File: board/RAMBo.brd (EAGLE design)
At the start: 104.1 x 102.9 mm, 262 parts, among them Q1 PSMN7R0-60YS, Q2 PSMN7R0-60YS, Q3 PSMN7R0-60YS, Q4 IRLML6346TRPBF, Q5 PSMN7R0-60YS, Q8 IRLML6346TRPBF, U1 ATMEGA32U2-MUR, U10 ADUM7441, U2 ATMEGA2560-16AU, U3 TPS54332DDA, U4 AD5206, U5 A4982, U6 A4982, U7 A4982, U8 A4982, U9 A4982, X1 C-GRID-02-70543, X10 C-GRID-04-70543, X11 MSTBV10, X12 SPI, X13 EXT-2, X14 C-GRID-04-70543, X15 C-GRID-04-70543, X16 32u2 EXT, X17 3x2M, X18 3x2M, X19 Analog-Ext, X2 USB B-TH, X20 M05PTH, X21 C-GRID-03-70543, X22 C-GRID-03-70543, X23 C-GRID-03-70543, X24 C-GRID-03-70543, X25 C-GRID-03-70543, X26 C-GRID-03-70543, X27 C-GRID-02-70543, X28 C-GRID-02-70543, X29 C-GRID-02-70543, X3 C-GRID-02-70543, X30 C-GRID-02-70543, X31 M05PTH, X32 M05PTH, X33 MSTBA6, X34 PWM_EXT, X39 M05X2PTH, X4 C-GRID-04-70543, X5 C-GRID-02-70543, X6 C-GRID-04-70543, X7 C-GRID-04-70543, X8 C-GRID-04-70543, X9 C-GRID-02-70543, Y1 16MHz KX-7, Y2 16MHz KX-7

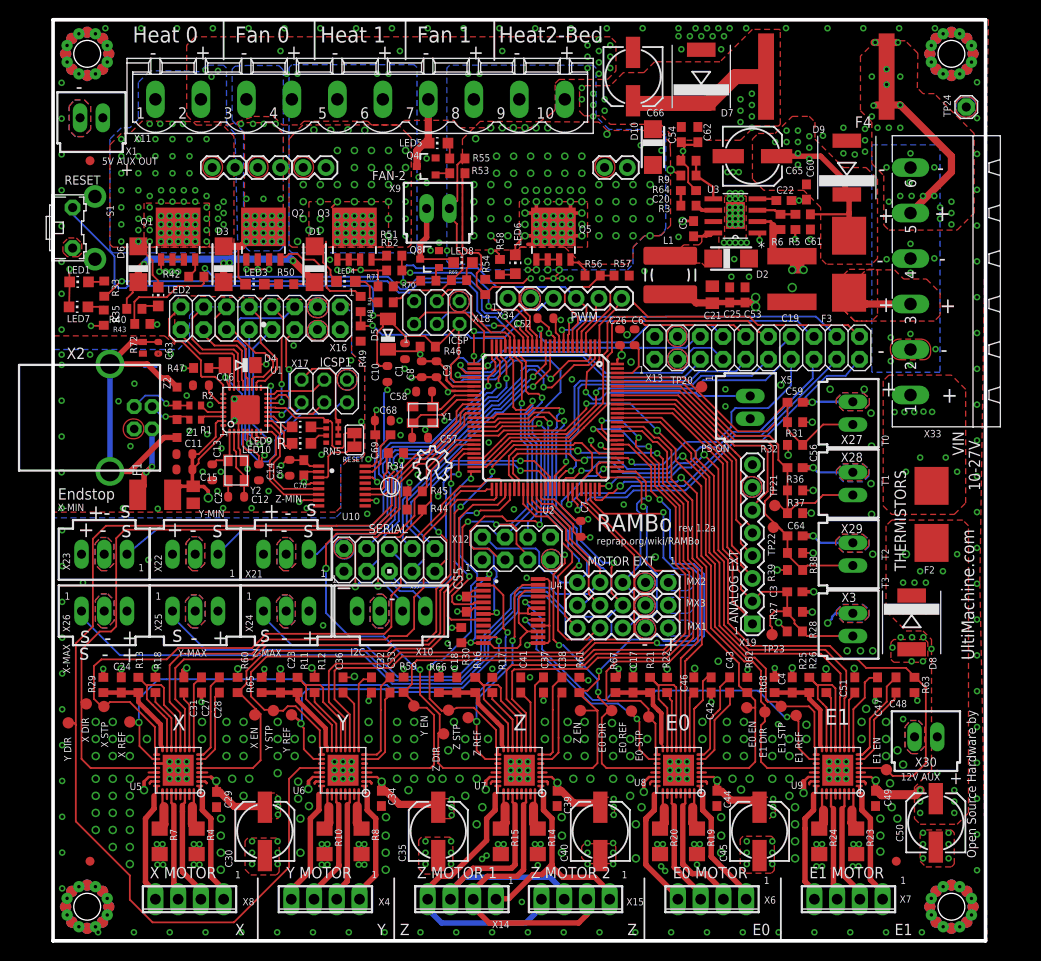
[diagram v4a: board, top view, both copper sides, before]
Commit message: remove solder pads under mount holes
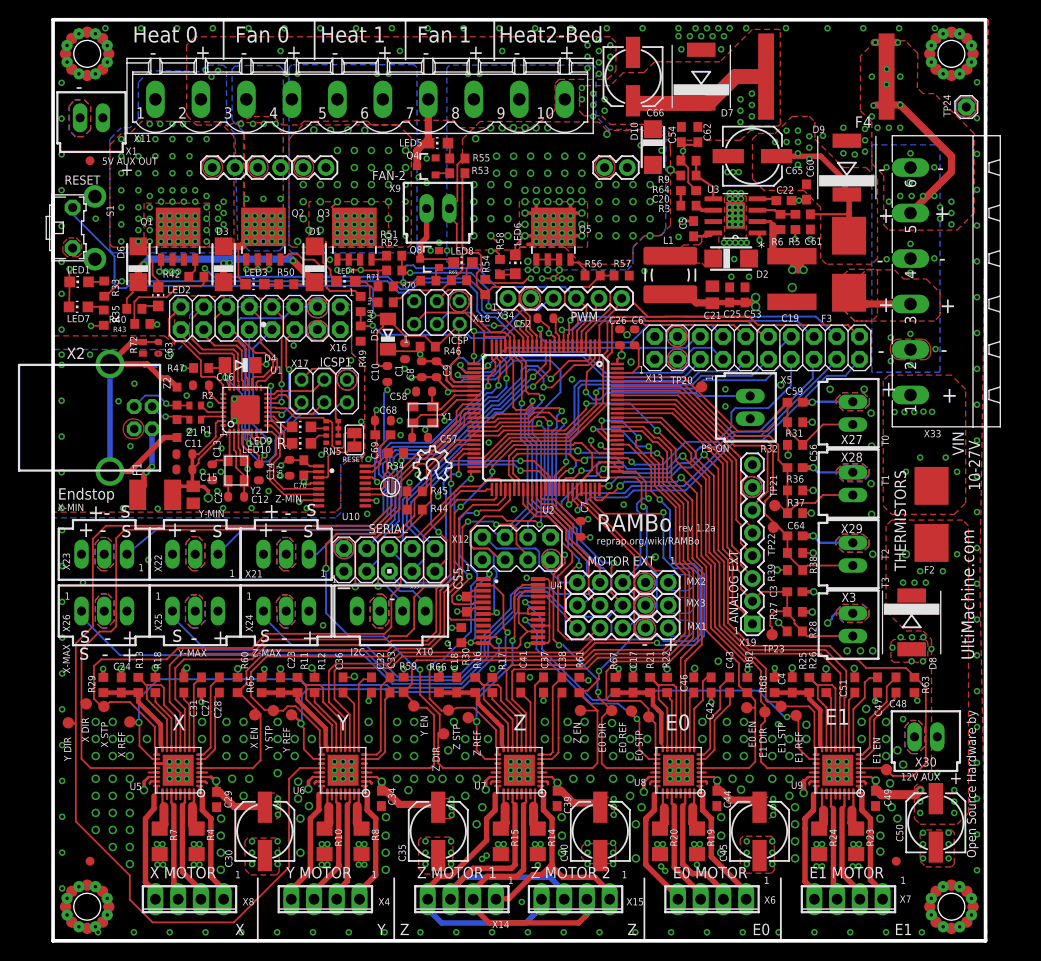
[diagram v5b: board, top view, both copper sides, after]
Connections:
- net GND: no longer H1.P$10, H1.P$11, H1.P$12, H1.P$13, H1.P$14, H1.P$15, H1.P$16, H1.P$9, H2.P$10, H2.P$11, H2.P$12, H2.P$13, H2.P$14, H2.P$15, H2.P$16, H2.P$9, H3.P$10, H3.P$11, H3.P$12, H3.P$13, H3.P$14, H3.P$15, H3.P$16, H3.P$9, H4.P$10, H4.P$11, H4.P$12, H4.P$13, H4.P$14, H4.P$15, H4.P$16, H4.P$9
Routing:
- net GND: vias 519 -> 520
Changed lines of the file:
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@@
 <grid distance="0.635" unitdist="mm" unit="mil" style="lines" multiple="1" display="no" altdistance="0.0635" altunitdist="mm" altunit="mm"/>
 <layers>
-<layer number="1" name="Top" color="4" fill="1" visible="yes" active="yes"/>
-<layer number="2" name="2-GND" color="13" fill="3" visible="yes" active="yes"/>
+<layer number="1" name="Top" color="4" fill="1" visible="no" active="yes"/>
+<layer number="2" name="2-GND" color="13" fill="3" visible="no" active="yes"/>
 <layer number="3" name="Route3" color="4" fill="3" visible="no" active="no"/>
 <layer number="14" name="Route14" color="1" fill="6" visible="no" active="no"/>
-<layer number="15" name="15-SUPPLY" color="11" fill="6" visible="yes" active="yes"/>
+<layer number="15" name="15-SUPPLY" color="11" fill="6" visible="no" active="yes"/>
 <layer number="16" name="Bottom" color="1" fill="1" visible="yes" active="yes"/>
 <layer number="17" name="Pads" color="2" fill="1" visible="yes" active="yes"/>
@@
 <contactref element="H1" pad="P$4"/>
 <contactref element="H1" pad="P$6"/>
-<contactref element="H1" pad="P$15"/>
 <contactref element="H1" pad="P$1"/>
-<contactref element="H1" pad="P$12"/>
-<contactref element="H1" pad="P$9"/>
 <contactref element="H1" pad="P$2"/>
-<contactref element="H1" pad="P$16"/>
 <contactref element="H1" pad="P$5"/>
-<contactref element="H1" pad="P$13"/>
-<contactref element="H1" pad="P$10"/>
 <contactref element="H1" pad="P$8"/>
 <contactref element="H1" pad="P$3"/>
 <contactref element="H1" pad="P$7"/>
-<contactref element="H1" pad="P$14"/>
-<contactref element="H1" pad="P$11"/>
 <contactref element="H2" pad="P$4"/>
 <contactref element="H2" pad="P$6"/>
-<contactref element="H2" pad="P$15"/>
 <contactref element="H2" pad="P$1"/>
-<contactref element="H2" pad="P$12"/>
-<contactref element="H2" pad="P$9"/>
 <contactref element="H2" pad="P$2"/>
-<contactref element="H2" pad="P$16"/>
 <contactref element="H2" pad="P$5"/>
-<contactref element="H2" pad="P$13"/>
-<contactref element="H2" pad="P$10"/>
 <contactref element="H2" pad="P$8"/>
 <contactref element="H2" pad="P$3"/>
 <contactref element="H2" pad="P$7"/>
-<contactref element="H2" pad="P$14"/>
-<contactref element="H2" pad="P$11"/>
 <contactref element="H3" pad="P$4"/>
 <contactref element="H3" pad="P$6"/>
-<contactref element="H3" pad="P$15"/>
 <contactref element="H3" pad="P$1"/>
-<contactref element="H3" pad="P$12"/>
-<contactref element="H3" pad="P$9"/>
 <contactref element="H3" pad="P$2"/>
-<contactref element="H3" pad="P$16"/>
 <contactref element="H3" pad="P$5"/>
-<contactref element="H3" pad="P$13"/>
-<contactref element="H3" pad="P$10"/>
 <contactref element="H3" pad="P$8"/>
 <contactref element="H3" pad="P$3"/>
 <contactref element="H3" pad="P$7"/>
-<contactref element="H3" pad="P$14"/>
-<contactref element="H3" pad="P$11"/>
 <contactref element="H4" pad="P$4"/>
 <contactref element="H4" pad="P$6"/>
-<contactref element="H4" pad="P$15"/>
 <contactref element="H4" pad="P$1"/>
-<contactref element="H4" pad="P$12"/>
-<contactref element="H4" pad="P$9"/>
 <contactref element="H4" pad="P$2"/>
-<contactref element="H4" pad="P$16"/>
 <contactref element="H4" pad="P$5"/>
-<contactref element="H4" pad="P$13"/>
-<contactref element="H4" pad="P$10"/>
 <contactref element="H4" pad="P$8"/>
 <contactref element="H4" pad="P$3"/>
 <contactref element="H4" pad="P$7"/>
-<contactref element="H4" pad="P$14"/>
-<contactref element="H4" pad="P$11"/>
 <polygon width="0.2032" layer="15" rank="4">
 <vertex x="0" y="102.87"/>
@@
 <via x="5.0275" y="0.9525" extent="1-16" drill="0.381"/>
 <via x="35.21075" y="53.7845" extent="1-16" drill="0.381"/>
+<via x="4.7625" y="80.6525" extent="1-16" drill="0.381"/>
 </signal>
 <signal name="VCC">

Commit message: rework psu layout, improve decoupling
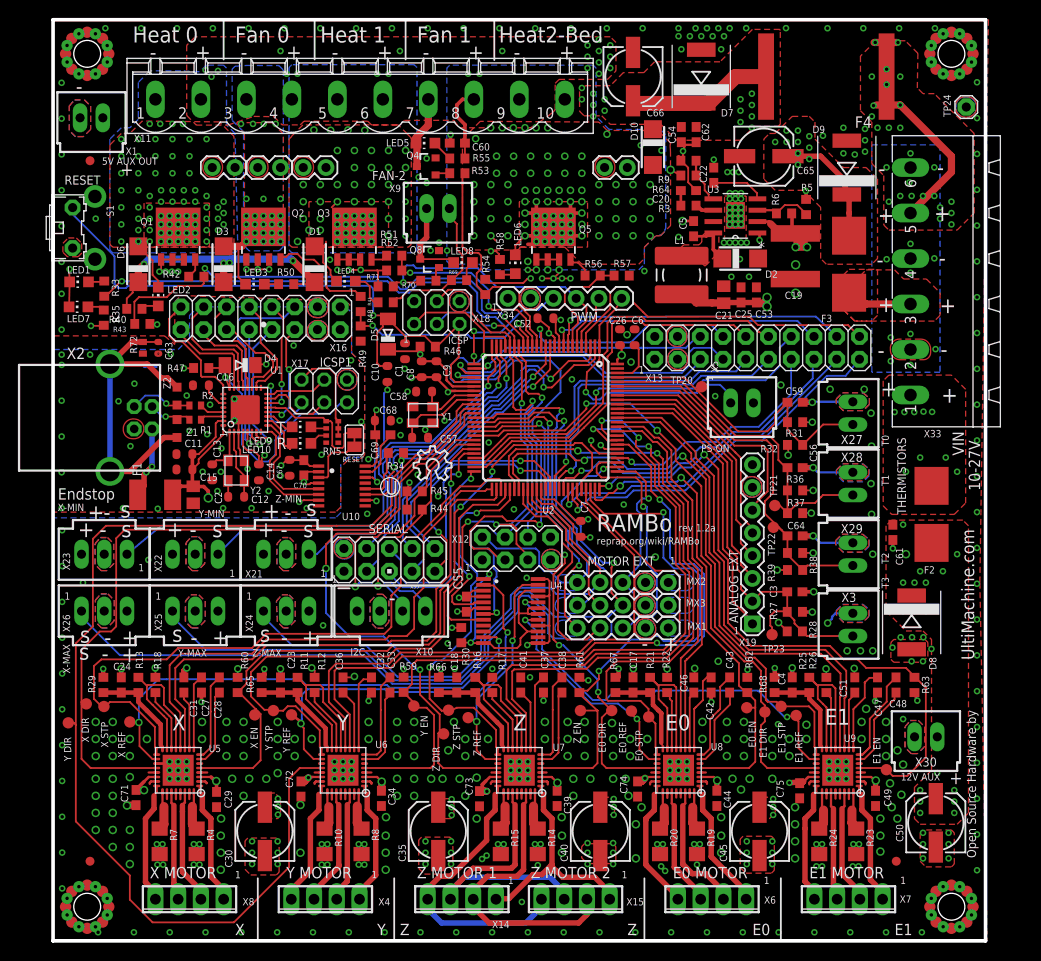
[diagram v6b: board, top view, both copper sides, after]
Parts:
- added C71, C72, C73, C74, C75: 100nF, resistor:C0603
- C60: value 10nF -> 100nF
- moved C60 39.4 mm to (45.1, 89.1), turned to 180 degrees
- moved C61 35.9 mm to (93.8, 45.6)
- moved C22 8.33 mm to (73.8, 85.5), turned to 90 degrees
- moved C19 2.57 mm to (82.9, 76.5)
- moved R5 2.05 mm to (84.1, 82.0), turned to 270 degrees
- moved LED5 1.46 mm to (41.6, 89.1)
- moved C21 1.27 mm to (74.9, 72.2)
- moved L1 1.27 mm to (70.2, 74.4)
- moved C25 1.27 mm to (76.8, 72.1)
- moved C53 1.27 mm to (78.5, 72.1)
- moved C65 1.27 mm to (79.4, 87.6)
- moved X5 1.04 mm to (76.9, 60.1), turned to 0 degrees
- moved R6 1.03 mm to (81.6, 81.2), turned to 0 degrees
- moved D2 1.02 mm to (76.7, 76.2)
- moved C62 0.19 mm to (71.8, 90.0)
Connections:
- net +12V: now also C61.1, C71.1, C72.1, C73.1, C74.1, C75.1
- net +12V2: no longer C61.1
- net GND: now also C71.2, C72.2, C73.2, C74.2, C75.2
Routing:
- net +12V: track 250.3 -> 177.9 mm, vias 46 -> 47
- net N$94: track 2.18 -> 5.96 mm
- net VCC: track 79.1 -> 82.6 mm
- net N$65: track 2.36 -> 5.63 mm
- net GND: track 142.8 -> 145.7 mm, vias 520 -> 518
- net N$97: track 4.39 -> 6.52 mm
- net +12V2: track 125.6 -> 124.7 mm
- net PG5: track 31.2 -> 30.5 mm
- net N$105: track 1.80 -> 2.40 mm
- added copper zone on layer 16, net PL3
- added copper zone on layer 16, net PL4
- added copper zone on layer 16, net PL5

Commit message: Add overvoltage protection to thermistor
based on nophead, bobc, NoobMan, Cefiar, and STB's discussion at
http://forums.reprap.org/read.php?13,197920,203564#msg-203564
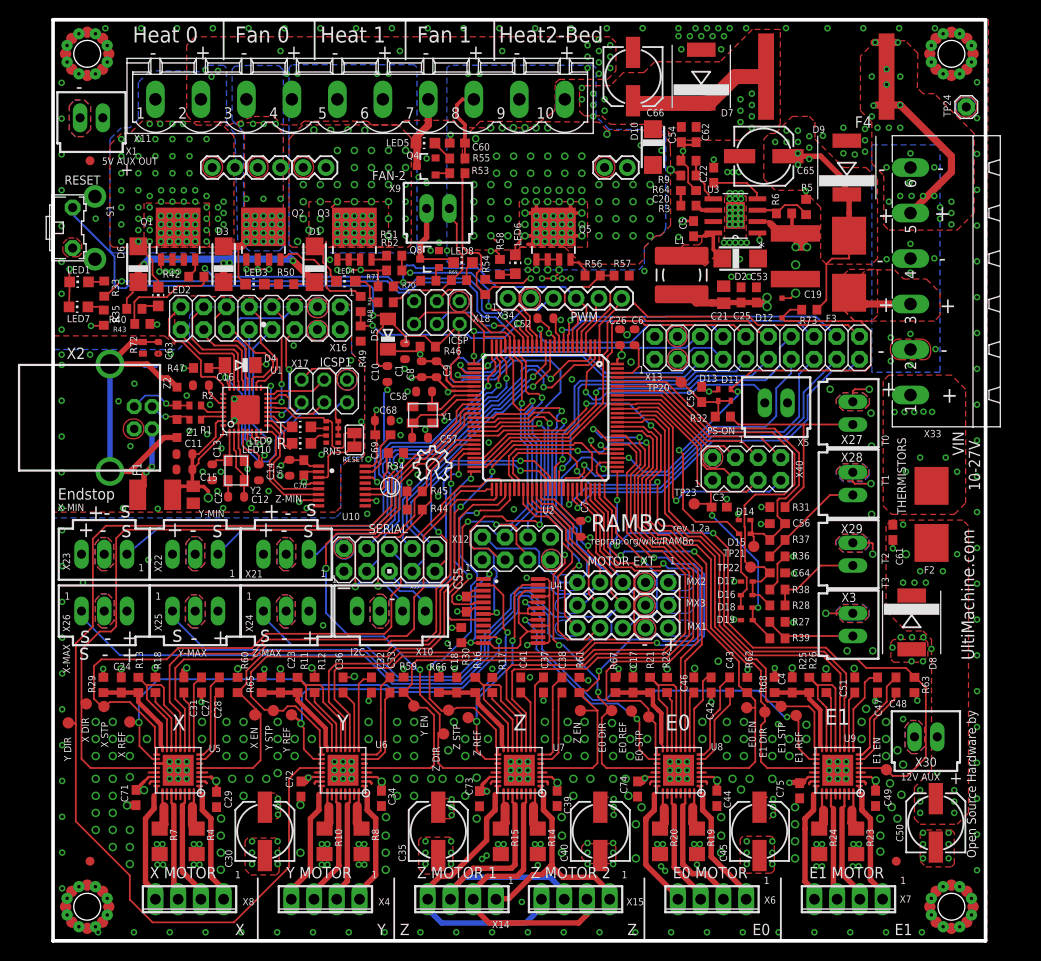
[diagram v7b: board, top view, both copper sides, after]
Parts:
- removed X19: Analog-Ext, SparkFun:1X08
- added D11, D13, D14, D15, D16, D17, D18, D19: 1N4148WT, diode:SOD523
- added D12: SZMM3Z4V7T1G, diode:SOD323-R
- added R73: 4K7, resistor:R0603
- added X40: Analog, SparkFun:2X4
- R28, R32, R37, R39: value CG0603MLC-05E -> 4K7
- moved TP23 17.0 mm to (71.6, 48.8)
- moved C3 12.7 mm to (74.4, 48.4)
- moved C59 10.5 mm to (72.4, 61.0), turned to 90 degrees
- moved R31 9.69 mm to (80.9, 48.4), turned to 180 degrees
- moved R32 8.66 mm to (74.8, 58.5)
- moved R39 7.88 mm to (80.9, 33.8)
- moved R36 7.62 mm to (80.9, 42.9)
- moved C56 6.55 mm to (80.9, 46.6), turned to 180 degrees
- moved TP21 5.14 mm to (78.3, 44.0)
- moved TP22 5.12 mm to (77.9, 41.7)
- moved C64 4.57 mm to (80.9, 41.1)
- moved R38 4.54 mm to (80.9, 39.2), turned to 180 degrees
- moved X5 3.81 mm to (80.8, 60.1)
- moved R37 3.59 mm to (80.9, 44.8)
- moved R28 3.49 mm to (80.9, 37.5)
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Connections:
- new net N$120: R27.1, R39.2, X3.2
- new net N$87: R31.1, R32.2, X27.2
- new net N$89: R36.1, R37.2, X28.2
- new net N$91: R28.2, R38.1, X29.2
- new net OVREF: D11.C, D12.C, D14.C, D16.C, D18.C, R73.1
- net +12V2: now also R73.2
- net ADC2: now also X40.3; no longer X19.3
- net ADC3: now also X40.4; no longer X19.4
- net ADC4: now also X40.6; no longer X19.5
- net ADC5: now also X40.8; no longer X19.6
- net GND: now also D12.A, D13.A, D15.A, D17.A, D19.A, X40.2; no longer R28.1, R32.1, R37.2, R39.1, X19.7
- net PK0: now also X40.7; no longer X19.1
- net THERM0: now also D11.A, D13.C, R32.1; no longer R31.1, R32.2, X27.2
- net THERM1: now also D14.A, D15.C; no longer R36.1, X28.2
- net THERM2: now also D16.A, D17.C, R28.1; no longer R38.1, R39.2, X29.2
- net THERM3: now also D18.A, D19.C, R39.1, X40.5; no longer R27.1, R28.2, X19.2, X3.2
- net VCC: now also X40.1; no longer X19.8
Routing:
- net OVREF: track 0.00 -> 67.0 mm, vias 0 -> 2
- net N$87: track 0.00 -> 24.1 mm
- net THERM0: track 36.7 -> 17.3 mm
- net N$89: track 0.00 -> 12.2 mm
- net ADC3: track 27.5 -> 15.9 mm
- net ADC2: track 29.5 -> 17.9 mm
- net +12V2: track 124.7 -> 135.6 mm
- net N$91: track 0.00 -> 10.4 mm
- net N$120: track 0.00 -> 10.2 mm
- net ADC4: track 25.6 -> 18.6 mm
- net THERM3: track 51.0 -> 44.6 mm, vias 0 -> 2
- net THERM2: track 43.0 -> 48.7 mm
- net ADC5: track 26.9 -> 21.3 mm
- net PK0: track 33.4 -> 28.0 mm, vias 0 -> 1
- net GND: track 145.7 -> 140.8 mm, vias 518 -> 512
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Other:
- board text removed: "ANALOG EXT"

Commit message: rework driver passives to make room for barcode
removed resistor on reset/sleep
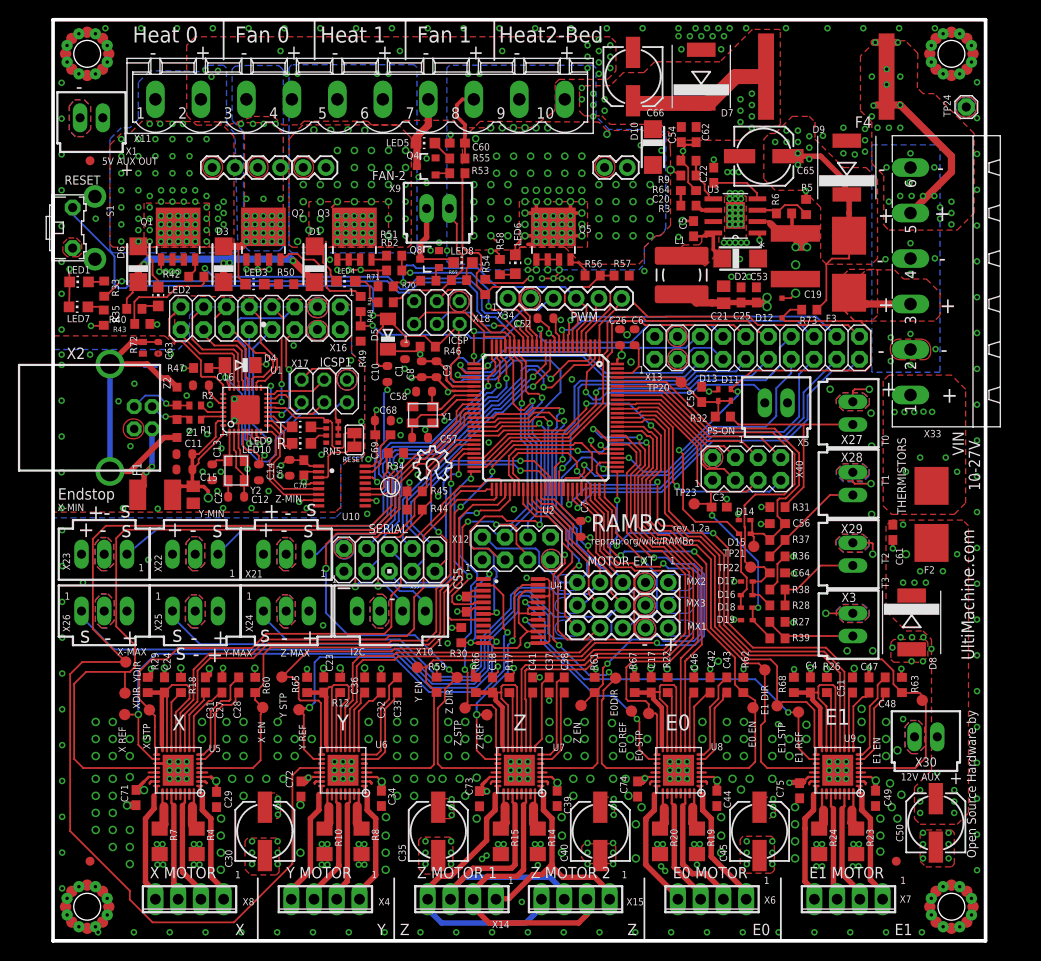
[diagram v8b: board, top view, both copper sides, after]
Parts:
- removed R11, R13, R16, R21, R25: 100K, resistor:R0603
- moved TP0 9.34 mm to (8.11, 31.1)
- moved TP18 8.72 mm to (97.1, 26.9)
- moved TP19 6.47 mm to (45.1, 29.4)
- moved TP2 5.09 mm to (10.8, 25.8)
- moved R65 5.08 mm to (28.4, 28.6)
- moved R29 4.95 mm to (10.6, 28.6)
- moved C23 4.83 mm to (30.2, 28.6)
- moved C24 4.83 mm to (12.4, 28.6)
- moved TP15 4.70 mm to (79.5, 30.3)
- moved TP1 4.48 mm to (8.03, 27.7)
- moved TP7 4.33 mm to (40.7, 30.5)
- moved R66 4.13 mm to (47.2, 28.6)
- moved C18 4.00 mm to (49.1, 28.6)
- moved TP5 3.87 mm to (25.6, 29.5)
- moved R59 3.68 mm to (42.8, 28.6)
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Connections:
- removed net N$111: C23.1, R11.1, R65.1, U6.16
- removed net N$112: C18.1, R16.1, R66.1, U7.16
- removed net N$115: C17.1, R21.1, R67.1, U8.16
- removed net N$116: C4.1, R25.1, R68.1, U9.16
- removed net N$27: R13.2, U5.13, U5.15
- net N$12: now also U5.13, U5.15; no longer R13.1
- net N$25: now also C23.1, R65.1, U6.16; no longer R11.2
- net N$44: now also C18.1, R66.1, U7.16; no longer R16.2
- net N$64: now also C17.1, R67.1, U8.16; no longer R21.2
- net N$77: now also C4.1, R68.1, U9.16; no longer R25.2
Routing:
- net N$27: track 18.7 -> 0.00 mm
- net N$12: track 11.3 -> 25.4 mm
- net N$111: track 11.7 -> 0.00 mm
- net N$112: track 11.7 -> 0.00 mm
- net N$116: track 10.7 -> 0.00 mm
- net N$115: track 10.7 -> 0.00 mm
- net X-STEP: track 75.9 -> 65.8 mm
- net +12V: track 177.9 -> 185.6 mm
- net N$77: track 18.3 -> 25.9 mm
- net N$64: track 18.4 -> 25.9 mm
- net X-DIR: track 84.9 -> 91.7 mm
- net N$44: track 19.3 -> 25.6 mm
- net Y-STEP: track 59.2 -> 53.2 mm
- net N$25: track 19.7 -> 25.7 mm
- net Y-DIR: track 131.1 -> 136.6 mm
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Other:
- board text added: "E0DIR"
- board text added: "XDIR"
- board text added: "YDIR"
- board text removed: "E0 DIR"
- board text removed: "X DIR"
- board text removed: "Y DIR"
